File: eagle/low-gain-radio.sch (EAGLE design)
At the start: 130 parts, among them U1 MKW01Z128, U2 SKY65116, U3 W25Q80DV, U4 LP5907MFX-3.3, U6 LP5907MFX-3.3, U7 LD39200, U8 MAAL-010704, Y1 32MHz

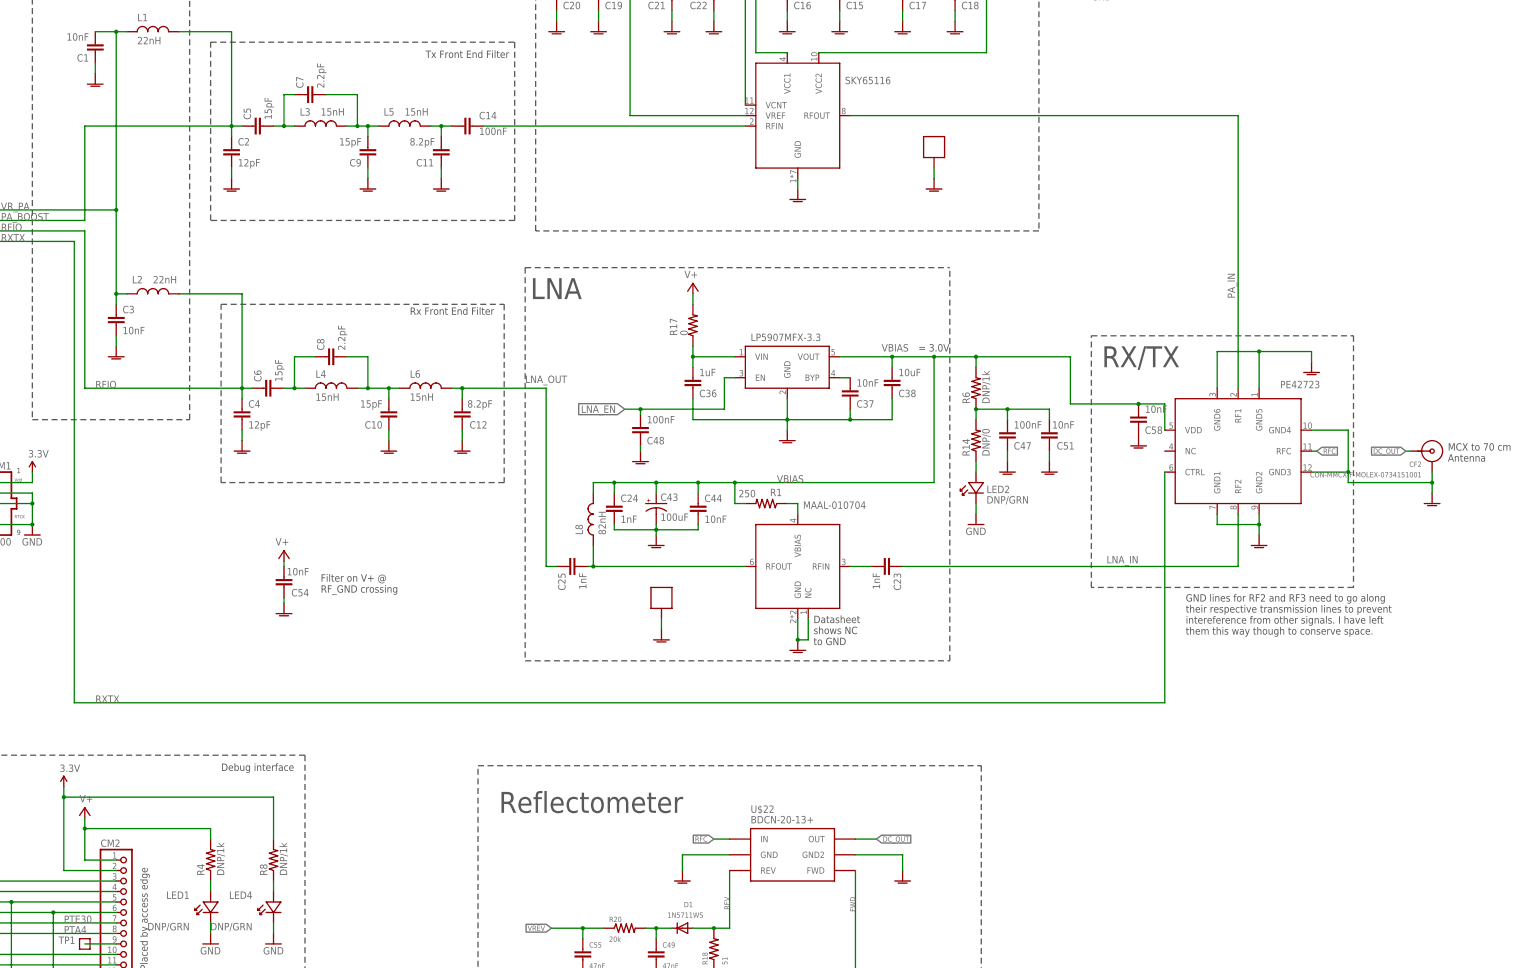
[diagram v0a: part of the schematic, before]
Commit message: added new RF switch, started layout but its unfinished, still need to hook GPIO to 40 pin connector as well
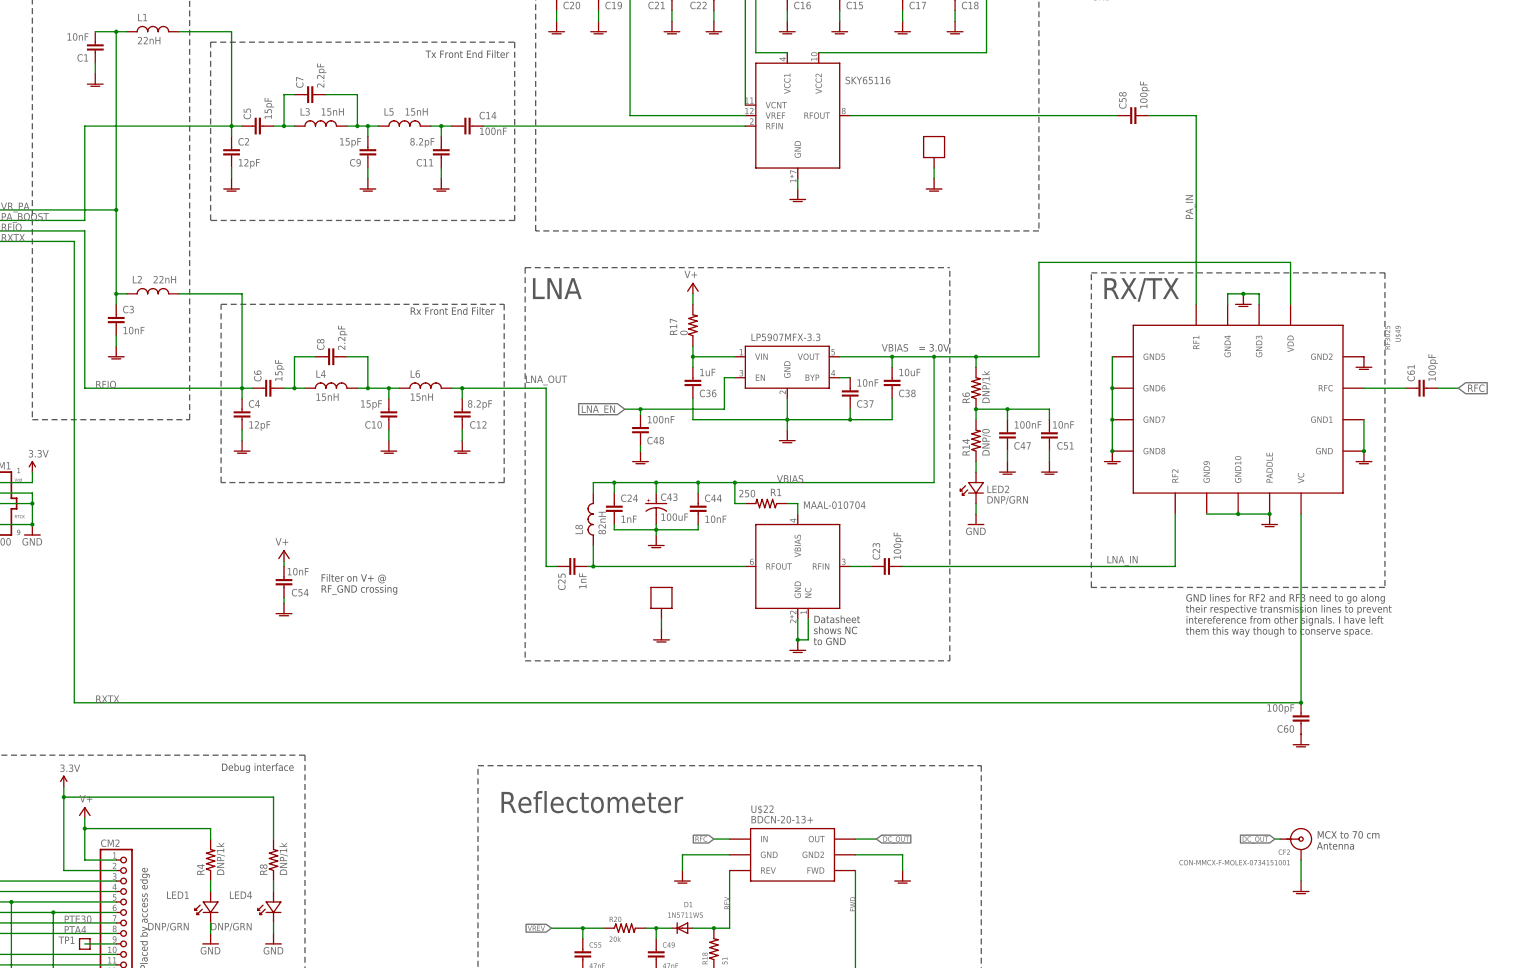
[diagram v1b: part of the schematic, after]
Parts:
- removed U$9: PE42723, low-gain-radio:PE42723
- added C60, C61: 100pF, low-gain-radio:C-EU0402-C-NOSILK
- added U$49: RF3025, low-gain-radio:RF3025
- C23: value 1nF -> 100pF; device rcl_custom:C-EU0402-B-NOSILK -> low-gain-radio:C-EU0402-C-NOSILK; DIST Digi-key -> Digi-Key Inc.; DPN 490-1303-1-ND -> 399-11246-2-ND; MFG Murata -> Kemet; MFG_PN GRM155R71H102KA01D -> (none); MPN (none) -> CBR04C101F3GAC
- C58: value 10nF -> 100pF; device rcl_custom:C-EU0603-B-NOSILK -> low-gain-radio:C-EU0402-C-NOSILK; DIST Digi-Key -> Digi-Key Inc.; DPN 490-1512-2-ND -> 399-11246-2-ND; MFG Murata -> Kemet; MFG_PN GRM188R71H103KA01D -> (none); MPN (none) -> CBR04C101F3GAC
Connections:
- new net RFOUT: C58.1, U2.RFOUT
- new net RXTX_OUT: C61.1, U$49.RFC
- net LNA_IN: now also C23.2, U$49.RF2; no longer C23.1, U$9.RF2
- net N$25: now also C23.1; no longer C23.2
- net PA_IN: now also C58.2, U$49.RF1; no longer U$9.RF1, U2.RFOUT
- net RFC: now also C61.2; no longer U$9.RFC
- net RF_GND: now also C60.1, U$49.GND, U$49.GND1, U$49.GND10, U$49.GND2, U$49.GND3, U$49.GND4, U$49.GND5, U$49.GND6, U$49.GND7, U$49.GND8, U$49.GND9, U$49.PADDLE; no longer C58.1, U$9.GND1, U$9.GND2, U$9.GND3, U$9.GND4, U$9.GND5, U$9.GND6
- net RXTX: now also C60.2, U$49.VC; no longer U$9.CTRL
- net VBIAS: now also U$49.VDD; no longer C58.2, U$9.VDD
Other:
- moved on the sheet: C23, C58, CF2

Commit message: added attributes to rf switch
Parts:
- U$49: DIST (none) -> Digi-Key Inc.; DPN (none) -> 689-1087-1-ND; MFG (none) -> RFMD; MPN (none) -> RF3025TR7
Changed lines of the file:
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@@
 <setting verticaltext="up"/>
 </settings>
-<grid distance="0.05" unitdist="inch" unit="inch" style="lines" multiple="1" display="yes" altdistance="0.01" altunitdist="inch" altunit="inch"/>
+<grid distance="0.1" unitdist="inch" unit="inch" style="lines" multiple="1" display="no" altdistance="0.01" altunitdist="inch" altunit="inch"/>
 <layers>
 <layer number="1" name="Top" color="4" fill="1" visible="no" active="no"/>
@@
 <part name="CF2" library="oresat-eagle" deviceset="CON-MMCX-F-MOLEX-0734151001" device=""/>
 <part name="RF-RESET" library="Tova" deviceset="TEST-POINT" device=""/>
-<part name="U$49" library="low-gain-radio" deviceset="RF3025" device=""/>
+<part name="U$49" library="low-gain-radio" deviceset="RF3025" device="">
+<attribute name="DIST" value="Digi-Key Inc."/>
+<attribute name="DPN" value="689-1087-1-ND"/>
+<attribute name="MFG" value="RFMD"/>
+<attribute name="MPN" value="RF3025TR7"/>
+</part>
 <part name="U$50" library="supply-rf_gnd" deviceset="RF_GND" device=""/>
 <part name="U$51" library="supply-rf_gnd" deviceset="RF_GND" device=""/>
@@
 <attribute name="NAME" x="45.72" y="154.94" size="1.778" layer="95" font="vector"/>
 </instance>
-<instance part="U$49" gate="G$1" x="487.68" y="185.42" rot="R270"/>
+<instance part="U$49" gate="G$1" x="487.68" y="185.42" rot="R270">
+<attribute name="MFG" x="487.68" y="185.42" size="1.778" layer="96" rot="R270" display="off"/>
+<attribute name="MPN" x="487.68" y="185.42" size="1.778" layer="96" rot="R270" display="off"/>
+<attribute name="DIST" x="487.68" y="185.42" size="1.778" layer="96" rot="R270" display="off"/>
+<attribute name="DPN" x="487.68" y="185.42" size="1.778" layer="96" rot="R270" display="off"/>
+</instance>
 <instance part="U$50" gate="1" x="488.95" y="210.82"/>
 <instance part="U$51" gate="1" x="457.2" y="172.72"/>

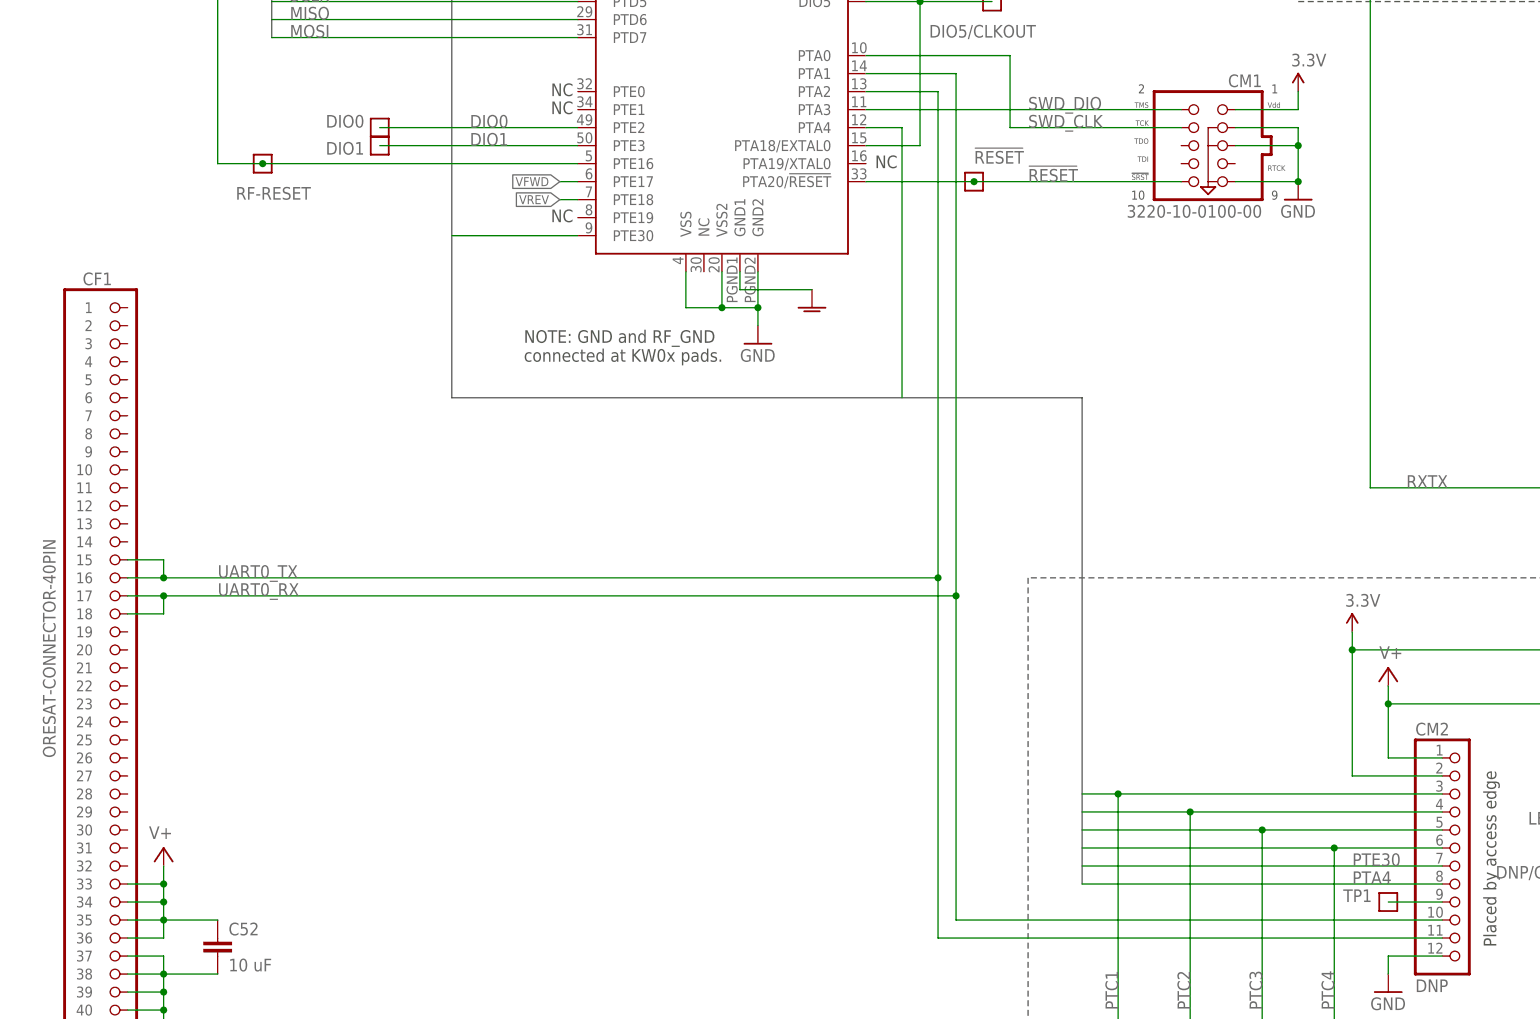
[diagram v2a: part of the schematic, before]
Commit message: finished with laying out the rf switch, placed and routed GPIO line for LLWU
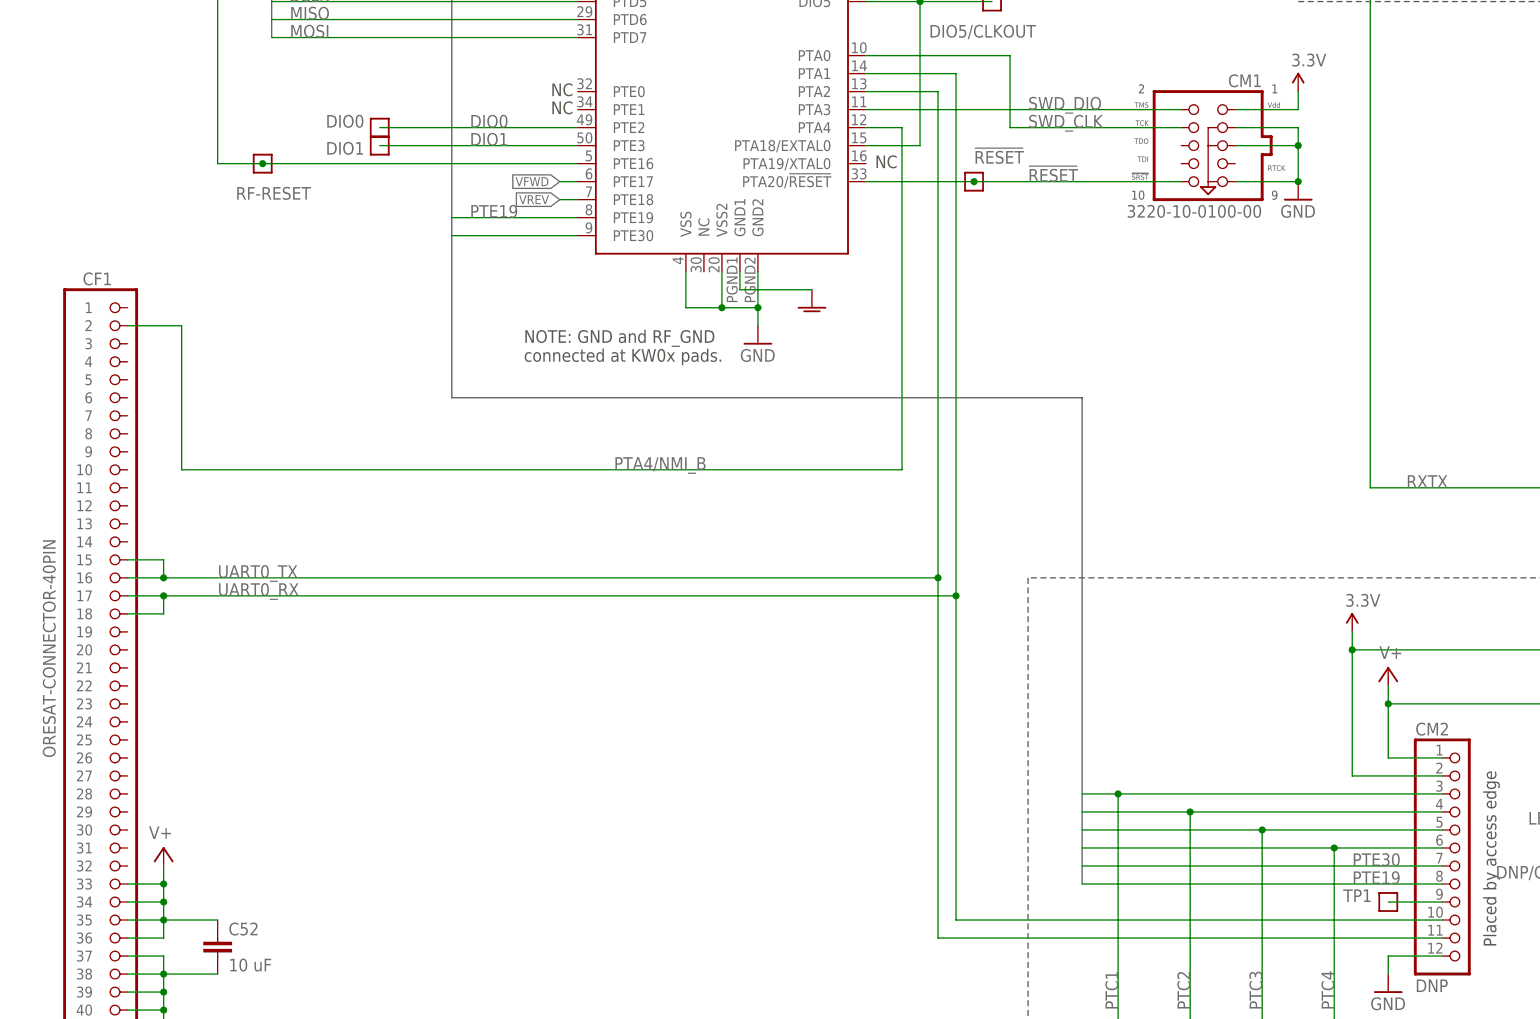
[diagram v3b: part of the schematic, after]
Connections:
- removed net PTA4: CM2.8, U1.PTA4
- new net PTA4/NMI_B: CF1.2, U1.PTA4
- new net PTE19: CM2.8, U1.PTE19
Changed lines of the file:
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@@
 <setting verticaltext="up"/>
 </settings>
-<grid distance="0.1" unitdist="inch" unit="inch" style="lines" multiple="1" display="no" altdistance="0.01" altunitdist="inch" altunit="inch"/>
+<grid distance="0.1" unitdist="inch" unit="inch" style="lines" multiple="1" display="yes" altdistance="0.01" altunitdist="inch" altunit="inch"/>
 <layers>
 <layer number="1" name="Top" color="4" fill="1" visible="no" active="no"/>
@@
 <text x="90.17" y="169.545" size="1.778" layer="97">NC</text>
 <text x="90.17" y="167.005" size="1.778" layer="97">NC</text>
-<text x="90.17" y="200.025" size="1.778" layer="97">NC</text>
 <text x="90.17" y="197.485" size="1.778" layer="97">NC</text>
 <text x="90.17" y="194.945" size="1.778" layer="97">NC</text>
 <text x="90.17" y="187.325" size="1.778" layer="97">NC</text>
 <text x="135.89" y="159.385" size="1.778" layer="97">NC</text>
-<text x="90.17" y="151.765" size="1.778" layer="97">NC</text>
 <wire x1="303.53" y1="99.06" x2="425.45" y2="99.06" width="0.1524" layer="97" style="longdash"/>
 <wire x1="425.45" y1="99.06" x2="425.45" y2="17.78" width="0.1524" layer="97" style="longdash"/>
@@
 <wire x1="303.53" y1="17.78" x2="303.53" y2="99.06" width="0.1524" layer="97" style="longdash"/>
 <text x="308.61" y="87.63" size="5.08" layer="97">Reflectometer</text>
+<text x="90.17" y="200.025" size="1.778" layer="97">NC</text>
 </plain>
 <instances>
@@
 </instances>
 <busses>
-<bus name="PTA4,PTB2,PTB17,PTC[1..7],PTD0,PTE[16..19],PTE30">
+<bus name="PTB2,PTB17,PTC[1..7],PTD0,PTE[16..19],PTE30">
 <segment>
 <wire x1="76.2" y1="210.82" x2="76.2" y2="127" width="0.762" layer="92"/>
@@
 </segment>
 </net>
-<net name="PTA4" class="0">
+<net name="PTA4/NMI_B" class="0">
 <segment>
-<wire x1="139.7" y1="127" x2="139.7" y2="165.1" width="0.1524" layer="91"/>
 <pinref part="U1" gate="G$1" pin="PTA4"/>
 <wire x1="139.7" y1="165.1" x2="134.62" y2="165.1" width="0.1524" layer="91"/>
-</segment>
-<segment>
-<pinref part="CM2" gate="G$1" pin="8"/>
-<wire x1="165.1" y1="58.42" x2="215.9" y2="58.42" width="0.1524" layer="91"/>
-<label x="203.2" y="58.42" size="1.778" layer="95"/>
+<wire x1="139.7" y1="165.1" x2="139.7" y2="116.84" width="0.1524" layer="91"/>
+<wire x1="139.7" y1="116.84" x2="38.1" y2="116.84" width="0.1524" layer="91"/>
+<wire x1="38.1" y1="116.84" x2="38.1" y2="137.16" width="0.1524" layer="91"/>
+<label x="99.06" y="116.84" size="1.778" layer="95"/>
+<pinref part="CF1" gate="G$1" pin="2"/>
+<wire x1="38.1" y1="137.16" x2="30.48" y2="137.16" width="0.1524" layer="91"/>
 </segment>
 </net>
@@
 </segment>
 </net>
+<net name="PTE19" class="0">
+<segment>
+<pinref part="U1" gate="G$1" pin="PTE19"/>
+<wire x1="93.98" y1="152.4" x2="76.2" y2="152.4" width="0.1524" layer="91"/>
+<label x="78.74" y="152.4" size="1.778" layer="95"/>
+</segment>
+<segment>
+<pinref part="CM2" gate="G$1" pin="8"/>
+<wire x1="165.1" y1="58.42" x2="215.9" y2="58.42" width="0.1524" layer="91"/>
+<label x="203.2" y="58.42" size="1.778" layer="95"/>
+</segment>
+</net>
